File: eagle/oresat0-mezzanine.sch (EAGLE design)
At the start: 23 parts, among them J1 R107064070, J10 R107064070, J2 R107064070, J3 R107064070, J4 R107064070, J5 R107064070, J6 R107064070, J7 R107064070, J8 R107064070, J9 R107064070, U1 QBA-07+, U2 QBA-07+, U3 QBA-07+, U7 QCN-27D+, U8 QCN-27D+, U9 QCN-27D+

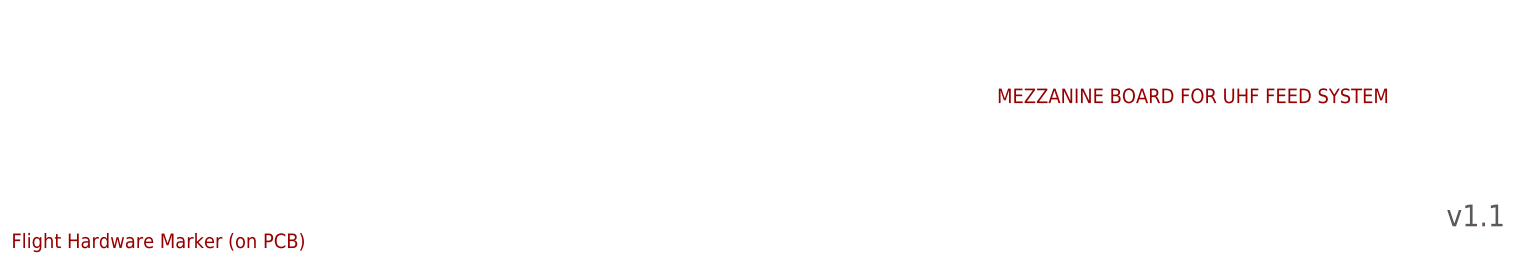
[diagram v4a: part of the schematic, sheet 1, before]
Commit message: Version 1.2 of the OreSat0 end card and mezzanine.
Largest change is the position of the antennas on the end card; changes to the deployer changed the antenna placement which triggered everything else.

Other changes include fiducials, attributes cleanup, move to 0603 resistors, and misc polish.
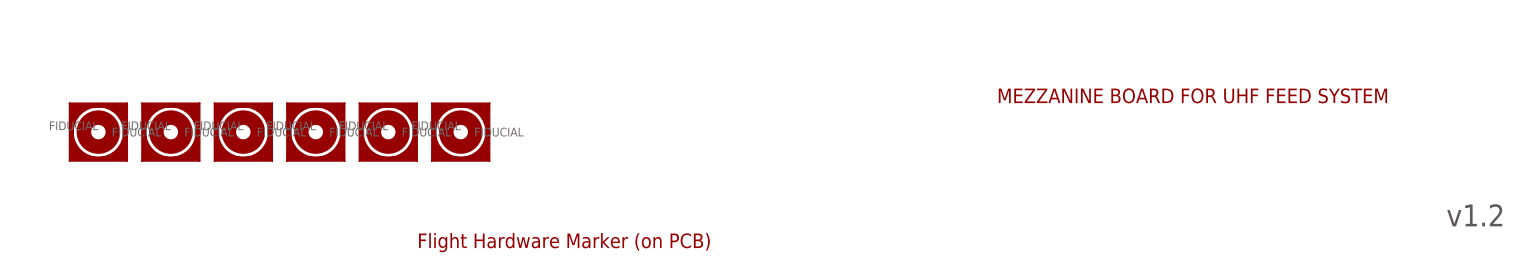
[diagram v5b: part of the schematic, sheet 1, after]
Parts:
- added FIDUCIAL1, FIDUCIAL2, FIDUCIAL3, FIDUCIAL4, FIDUCIAL6, FIDUCIAL7: FIDUCIAL-1.0X2.0, monitor-v2-debug:FIDUCIAL-1.0X2.0
- R1, R2, R3, R4, R5, R6: device oresat-rcl:R-US_0805-B-NOSILK -> oresat-rcl:R-US_0603-C-NOSILK
- U7, U8, U9: value QCN-27D+ -> QCN-27+
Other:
- note added: "v1.2"
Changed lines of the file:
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@@
 <?xml version="1.0" encoding="utf-8"?>
 <!DOCTYPE eagle SYSTEM "eagle.dtd">
-<eagle version="9.6.1">
+<eagle version="9.6.2">
 <drawing>
 <settings>
@@
 <part name="GND9" library="supply1" library_urn="urn:adsk.eagle:library:371" deviceset="GND" device=""/>
 <part name="GND10" library="supply1" library_urn="urn:adsk.eagle:library:371" deviceset="GND" device=""/>
-<part name="R1" library="oresat-rcl" deviceset="R-US_" device="0805-B-NOSILK" value="50"/>
-<part name="R2" library="oresat-rcl" deviceset="R-US_" device="0805-B-NOSILK" value="50"/>
-<part name="R3" library="oresat-rcl" deviceset="R-US_" device="0805-B-NOSILK" value="50"/>
+<part name="R1" library="oresat-rcl" deviceset="R-US_" device="0603-C-NOSILK" value="50"/>
+<part name="R2" library="oresat-rcl" deviceset="R-US_" device="0603-C-NOSILK" value="50"/>
+<part name="R3" library="oresat-rcl" deviceset="R-US_" device="0603-C-NOSILK" value="50"/>
 <part name="J1" library="J-Radiall-R107064070-RF" deviceset="R107064070" device=""/>
 <part name="J2" library="J-Radiall-R107064070-RF" deviceset="R107064070" device=""/>
@@
 <part name="GND21" library="supply1" library_urn="urn:adsk.eagle:library:371" deviceset="GND" device=""/>
 <part name="GND22" library="supply1" library_urn="urn:adsk.eagle:library:371" deviceset="GND" device=""/>
-<part name="R4" library="oresat-rcl" deviceset="R-US_" device="0805-B-NOSILK" value="50"/>
-<part name="R5" library="oresat-rcl" deviceset="R-US_" device="0805-B-NOSILK" value="50"/>
-<part name="R6" library="oresat-rcl" deviceset="R-US_" device="0805-B-NOSILK" value="50"/>
+<part name="R4" library="oresat-rcl" deviceset="R-US_" device="0603-C-NOSILK" value="50"/>
+<part name="R5" library="oresat-rcl" deviceset="R-US_" device="0603-C-NOSILK" value="50"/>
+<part name="R6" library="oresat-rcl" deviceset="R-US_" device="0603-C-NOSILK" value="50"/>
 <part name="J6" library="J-Radiall-R107064070-RF" deviceset="R107064070" device=""/>
 <part name="J7" library="J-Radiall-R107064070-RF" deviceset="R107064070" device=""/>
@@
 <part name="J9" library="J-Radiall-R107064070-RF" deviceset="R107064070" device=""/>
 <part name="J10" library="J-Radiall-R107064070-RF" deviceset="R107064070" device=""/>
-<part name="U7" library="U-MiniCirc-QCN-XXX+-quad" deviceset="QCN-XXX+" device="" value="QCN-27D+"/>
-<part name="U8" library="U-MiniCirc-QCN-XXX+-quad" deviceset="QCN-XXX+" device="" value="QCN-27D+"/>
-<part name="U9" library="U-MiniCirc-QCN-XXX+-quad" deviceset="QCN-XXX+" device="" value="QCN-27D+"/>
+<part name="U7" library="U-MiniCirc-QCN-XXX+-quad" deviceset="QCN-XXX+" device="" value="QCN-27+"/>
+<part name="U8" library="U-MiniCirc-QCN-XXX+-quad" deviceset="QCN-XXX+" device="" value="QCN-27+"/>
+<part name="U9" library="U-MiniCirc-QCN-XXX+-quad" deviceset="QCN-XXX+" device="" value="QCN-27+"/>
 <part name="U$1" library="oresat-flight-marker" deviceset="FLIGHMARKER" device="NEW"/>
+<part name="FIDUCIAL2" library="monitor-v2-debug" deviceset="FIDUCIAL" device="-1.0X2.0"/>
+<part name="FIDUCIAL3" library="monitor-v2-debug" deviceset="FIDUCIAL" device="-1.0X2.0"/>
+<part name="FIDUCIAL4" library="monitor-v2-debug" deviceset="FIDUCIAL" device="-1.0X2.0"/>
+<part name="FIDUCIAL6" library="monitor-v2-debug" deviceset="FIDUCIAL" device="-1.0X2.0"/>
+<part name="FIDUCIAL7" library="monitor-v2-debug" deviceset="FIDUCIAL" device="-1.0X2.0"/>
+<part name="FIDUCIAL1" library="monitor-v2-debug" deviceset="FIDUCIAL" device="-1.0X2.0"/>
 </parts>
 <sheets>
@@
 <plain>
 <text x="119.38" y="88.9" size="1.778" layer="97">1/4 wavelength</text>
-<text x="261.62" y="6.35" size="3.81" layer="97">v1.1</text>
+<text x="261.62" y="6.35" size="3.81" layer="97">v1.2</text>
 <text x="182.88" y="27.94" size="2.54" layer="94">MEZZANINE BOARD FOR UHF FEED SYSTEM</text>
 <text x="200.66" y="66.04" size="1.778" layer="97">MAKE SAME LENGTH</text>
@@
 <attribute name="VALUE" x="231.14" y="76.2" size="1.778" layer="96"/>
 </instance>
-<instance part="U$1" gate="G$1" x="10.16" y="2.54" smashed="yes"/>
+<instance part="U$1" gate="G$1" x="81.28" y="2.54" smashed="yes"/>
+<instance part="FIDUCIAL2" gate="FIDUCIAL" x="25.4" y="22.86" smashed="yes"/>
+<instance part="FIDUCIAL3" gate="FIDUCIAL" x="38.1" y="22.86" smashed="yes"/>
+<instance part="FIDUCIAL4" gate="FIDUCIAL" x="50.8" y="22.86" smashed="yes"/>
+<instance part="FIDUCIAL6" gate="FIDUCIAL" x="63.5" y="22.86" smashed="yes"/>
+<instance part="FIDUCIAL7" gate="FIDUCIAL" x="76.2" y="22.86" smashed="yes"/>
+<instance part="FIDUCIAL1" gate="FIDUCIAL" x="88.9" y="22.86" smashed="yes"/>
 </instances>
 <busses>
@@
 </segment>
 </net>
-<net name="N$3" class="1">
+<net name="N$3" class="0">
 <segment>
 <pinref part="U1" gate="G$1" pin="TERM"/>
@@
 </segment>
 </net>
-<net name="N$4" class="1">
+<net name="N$4" class="0">
 <segment>
 <pinref part="U2" gate="G$1" pin="TERM"/>
@@
 </segment>
 </net>
-<net name="N$6" class="1">
+<net name="N$6" class="0">
 <segment>
 <pinref part="U3" gate="G$1" pin="TERM"/>
@@
 </busses>
 <nets>
-<net name="N$1" class="1">
+<net name="N$1" class="0">
 <segment>
 <wire x1="-172.72" y1="271.78" x2="-180.34" y2="271.78" width="0.1524" layer="91"/>
@@
 </segment>
 </net>
-<net name="N$2" class="1">
+<net name="N$2" class="0">
 <segment>
 <wire x1="-93.98" y1="289.56" x2="-101.6" y2="289.56" width="0.1524" layer="91"/>
@@
 </segment>
 </net>
-<net name="N$5" class="1">
+<net name="N$5" class="0">
 <segment>
 <wire x1="-93.98" y1="238.76" x2="-101.6" y2="238.76" width="0.1524" layer="91"/>
